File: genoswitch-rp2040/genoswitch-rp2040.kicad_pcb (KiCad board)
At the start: 2 copper layers, 37 parts, among them J1 USB_B_Micro, J2 Conn_01x03_Socket-PicoDebug, J3 HW-SPI0, J4 HW-SPI1, J5 PIO-SPI0, J6 PIO-SPI1, J7 SERIAL, SW1 PTS815_SJM_250_SMTR_LFS, U1 NCP1117-3.3_SOT223, U2 W25Q128JVS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

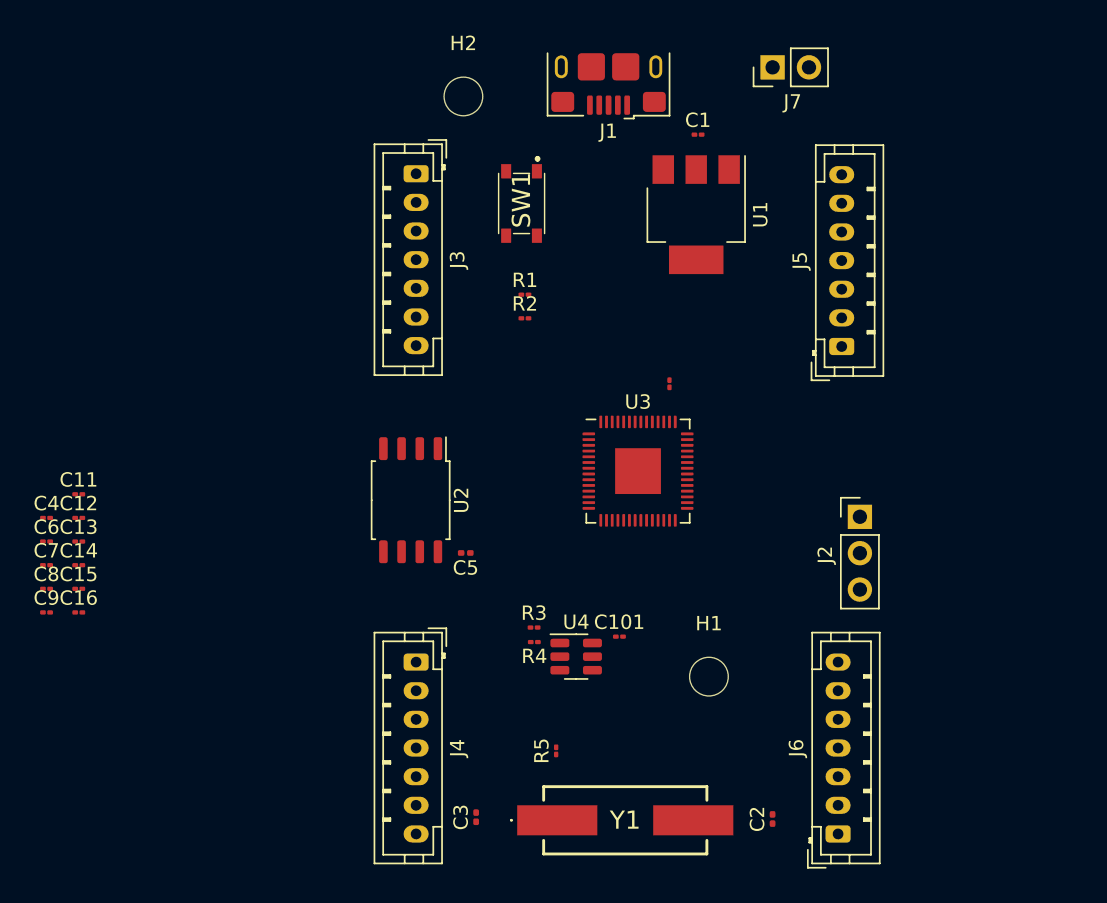
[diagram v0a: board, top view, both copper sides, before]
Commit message: Place all components in rough positions
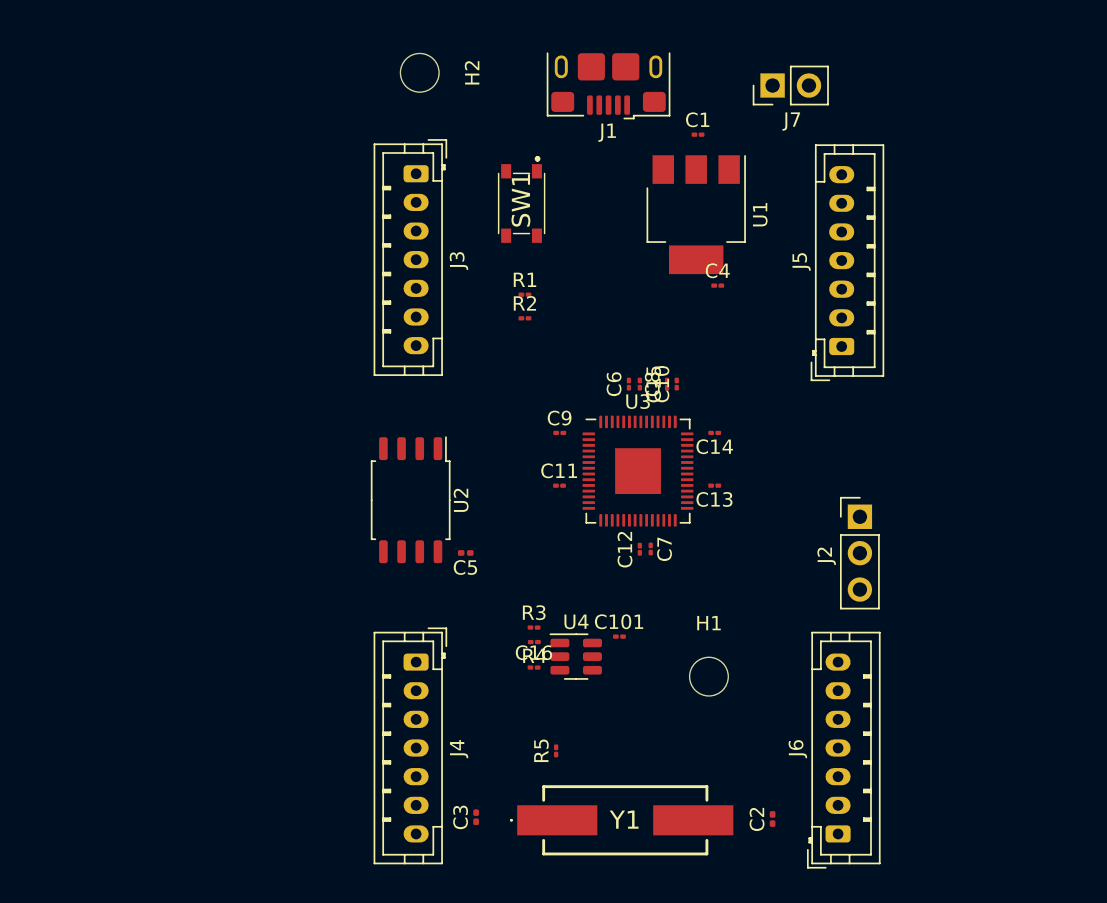
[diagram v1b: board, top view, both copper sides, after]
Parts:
- moved C4 49.6 mm to (114.9, 61.0)
- moved C8 45.6 mm to (111.4, 67.8), turned to 90 degrees
- moved C14 45.4 mm to (114.7, 71.2), turned to 180 degrees
- moved C13 44.6 mm to (114.7, 74.9), turned to 180 degrees
- moved C7 42.2 mm to (110.2, 79.4), turned to -90 degrees
- moved C6 42.1 mm to (108.7, 67.8), turned to 90 degrees
- moved C15 41.7 mm to (109.5, 67.8), turned to -90 degrees
- moved C12 39.2 mm to (109.5, 79.4), turned to 90 degrees
- moved C9 38.0 mm to (103.9, 71.2)
- moved C11 33.6 mm to (103.9, 74.9)
- moved C16 32.0 mm to (102.1, 87.6)
- moved H2 3.47 mm to (94.1, 46.1), turned to -90 degrees
- moved J7 1.27 mm to (118.7, 47.0)
- moved C10 0.51 mm to (112.1, 67.8)

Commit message: Swap to horizonal JST PH connector
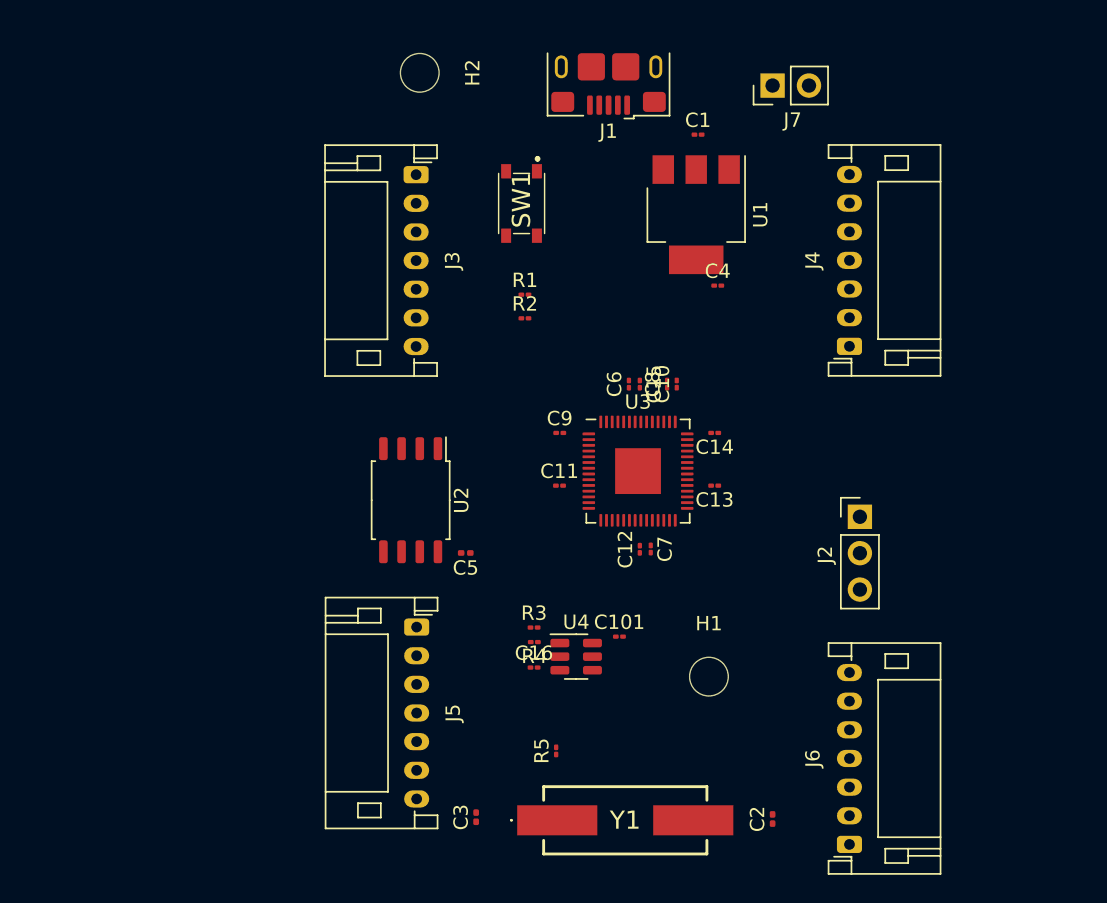
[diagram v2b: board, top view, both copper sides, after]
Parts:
- J3, J4, J5, J6: footprint Connector_JST:JST_PH_B7B-PH-K_1x07_P2.00mm_Vertical -> Connector_JST:JST_PH_S7B-PH-K_1x07_P2.00mm_Horizontal
- moved J4 37.4 mm to (124.1, 65.2), turned to 90 degrees
- moved J5 35.6 mm to (93.9, 84.8), turned to -90 degrees
- moved J6 1.08 mm to (124.1, 100.0)
- moved J3 0.06 mm to (93.9, 53.2)

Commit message: Route USB Data Lines
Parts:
- moved C15 26.3 mm to (135.8, 68.3)
- moved C6 26.3 mm to (135.1, 68.3)
- moved C8 26.3 mm to (137.7, 68.3)
- moved C10 26.3 mm to (138.4, 68.3)
- moved U1 2.13 mm to (115.2, 57.1)
- moved C1 1.44 mm to (114.3, 51.6)
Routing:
- net /USB_D+: track 0.00 -> 23.5 mm
- net /USB_D-: track 0.00 -> 23.5 mm
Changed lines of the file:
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@@
   )
   (footprint "Capacitor_SMD:C_01005_0402Metric" (layer "F.Cu")
-    (at 112.052 67.835 90)
+    (at 138.39 68.321 90)
     (descr "Capacitor SMD 01005 (0402 Metric), square (rectangular) end terminal, IPC_7351 nominal, (Body size source: http://www.vishay.com/docs/20056/crcw01005e3.pdf), generated with kicad-footprint-generator")
     (tags "capacitor")
@@
   )
   (footprint "Capacitor_SMD:C_01005_0402Metric" (layer "F.Cu")
-    (at 108.712 67.839 90)
+    (at 135.05 68.325 90)
     (descr "Capacitor SMD 01005 (0402 Metric), square (rectangular) end terminal, IPC_7351 nominal, (Body size source: http://www.vishay.com/docs/20056/crcw01005e3.pdf), generated with kicad-footprint-generator")
     (tags "capacitor")
@@
   )
   (footprint "Capacitor_SMD:C_01005_0402Metric" (layer "F.Cu")
-    (at 109.474 67.839 -90)
+    (at 135.812 68.325 -90)
     (descr "Capacitor SMD 01005 (0402 Metric), square (rectangular) end terminal, IPC_7351 nominal, (Body size source: http://www.vishay.com/docs/20056/crcw01005e3.pdf), generated with kicad-footprint-generator")
     (tags "capacitor")
@@
   )
   (footprint "Package_TO_SOT_SMD:SOT-223-3_TabPin2" (layer "F.Cu")
-    (at 113.411 56.007 -90)
+    (at 115.212 57.15 -90)
     (descr "module CMS SOT223 4 pins")
     (tags "CMS SOT")
@@
   )
   (footprint "Capacitor_SMD:C_01005_0402Metric" (layer "F.Cu")
-    (at 113.538 50.419)
+    (at 114.287 51.65)
     (descr "Capacitor SMD 01005 (0402 Metric), square (rectangular) end terminal, IPC_7351 nominal, (Body size source: http://www.vishay.com/docs/20056/crcw01005e3.pdf), generated with kicad-footprint-generator")
     (tags "capacitor")
@@
   )
   (footprint "Capacitor_SMD:C_01005_0402Metric" (layer "F.Cu")
-    (at 111.379 67.839 90)
+    (at 137.717 68.325 90)
     (descr "Capacitor SMD 01005 (0402 Metric), square (rectangular) end terminal, IPC_7351 nominal, (Body size source: http://www.vishay.com/docs/20056/crcw01005e3.pdf), generated with kicad-footprint-generator")
     (tags "capacitor")
@@
     (property "ki_keywords" "RP2040 ARM Cortex-M0+ USB")
     (attr smd)
-    (fp_text reference "U3" (at 0 -4.82) (layer "F.SilkS")
+    (fp_text reference "U3" (at 26.338 -4.334) (layer "F.SilkS")
         (effects (font (size 1 1) (thickness 0.15)))
     )
@@
     (stroke (width 0.15) (type default)) (layer "User.1"))
   (segment (start 111.544 70.4735) (end 111.547 70.4765) (width 0.15) (layer "F.Cu") (net 7))
+  (segment (start 108.162 50) (end 108.162 64.97655) (width 0.8) (layer "F.Cu") (net 10))
+  (segment (start 107.94 48.358) (end 107.94 49.778) (width 0.1524) (layer "F.Cu") (net 10))
+  (segment (start 108.162 64.97655) (end 110.965231 67.779781) (width 0.8) (layer "F.Cu") (net 10))
+  (segment (start 107.94 49.778) (end 108.162 50) (width 0.1524) (layer "F.Cu") (net 10))
+  (segment (start 110.747 70.4765) (end 110.747 69.326447) (width 0.1524) (layer "F.Cu") (net 10))
+  (segment (start 110.965231 67.779781) (end 110.965231 69.108216) (width 0.8) (layer "F.Cu") (net 10))
+  (segment (start 110.747 69.326447) (end 110.965231 69.108216) (width 0.1524) (layer "F.Cu") (net 10))
+  (segment (start 110.347 70.4765) (end 110.347 69.442385) (width 0.1524) (layer "F.Cu") (net 11))
+  (segment (start 110.347 69.442385) (end 110.012831 69.108216) (width 0.1524) (layer "F.Cu") (net 11))
+  (segment (start 107.112 65.27345) (end 110.012831 68.174281) (width 0.8) (layer "F.Cu") (net 11))
+  (segment (start 110.012831 68.174281) (end 110.012831 69.108216) (width 0.8) (layer "F.Cu") (net 11))
+  (segment (start 107.112 50) (end 107.112 65.27345) (width 0.8) (layer "F.Cu") (net 11))
+  (segment (start 107.29 48.358) (end 107.29 49.822) (width 0.1524) (layer "F.Cu") (net 11))
+  (segment (start 107.29 49.822) (end 107.112 50) (width 0.1524) (layer "F.Cu") (net 11))
 )

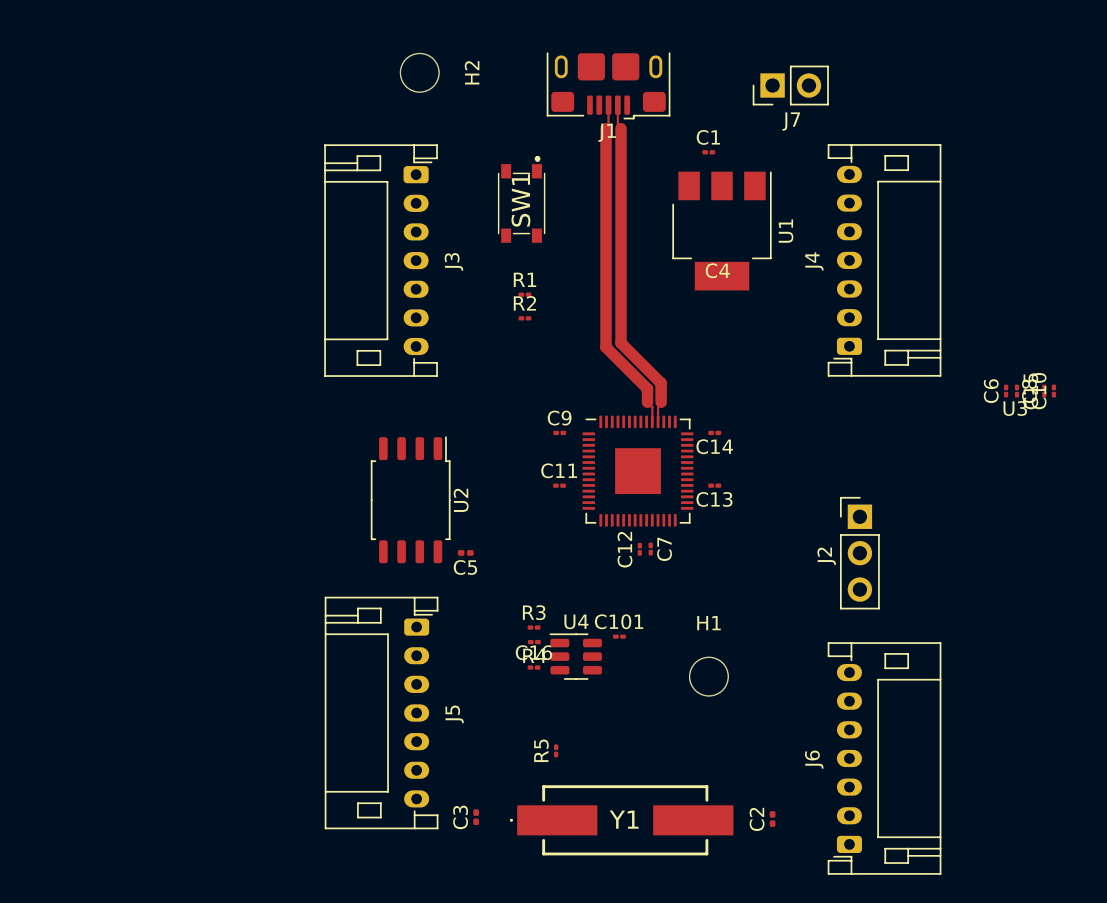
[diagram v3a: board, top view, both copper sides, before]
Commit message: move components, slight routing
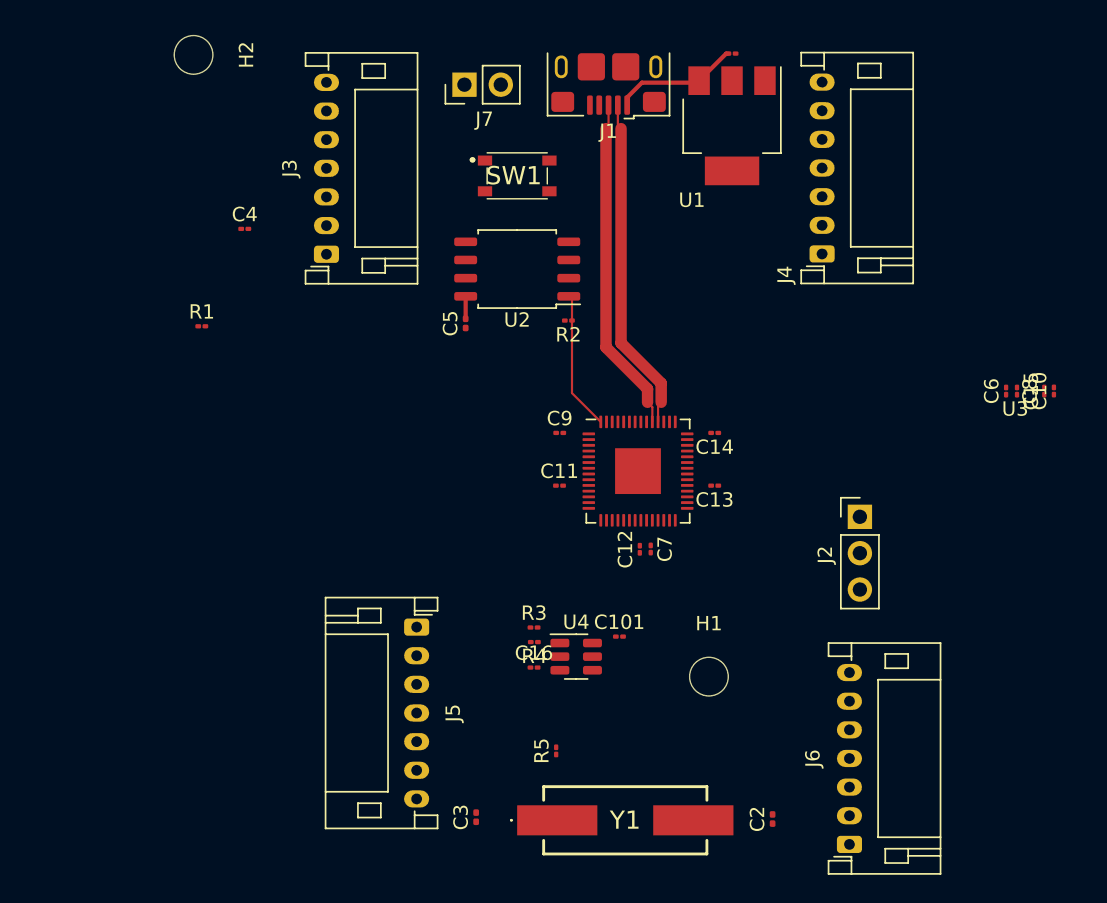
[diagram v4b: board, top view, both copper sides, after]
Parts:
- moved C4 33.3 mm to (81.9, 57.0)
- moved R1 22.7 mm to (78.9, 63.8)
- moved J7 21.5 mm to (97.2, 46.9)
- moved U2 17.8 mm to (100.9, 59.8), turned to 180 degrees
- moved C5 16.0 mm to (97.3, 63.6), turned to 90 degrees
- moved H2 15.8 mm to (78.3, 44.9)
- moved J3 8.37 mm to (87.6, 58.8), turned to 90 degrees
- moved U1 7.38 mm to (115.9, 49.8)
- moved C1 7.08 mm to (115.9, 44.8)
- moved J4 6.73 mm to (122.2, 58.8)
- moved R2 3.04 mm to (104.5, 63.4), turned to 180 degrees
- moved SW1 1.95 mm to (100.9, 53.3), turned to 0 degrees
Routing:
- net /QSPI_SS: track 0.00 -> 9.69 mm
- net VBUS: track 0.00 -> 8.88 mm
- net +3V3: track 0.00 -> 1.57 mm

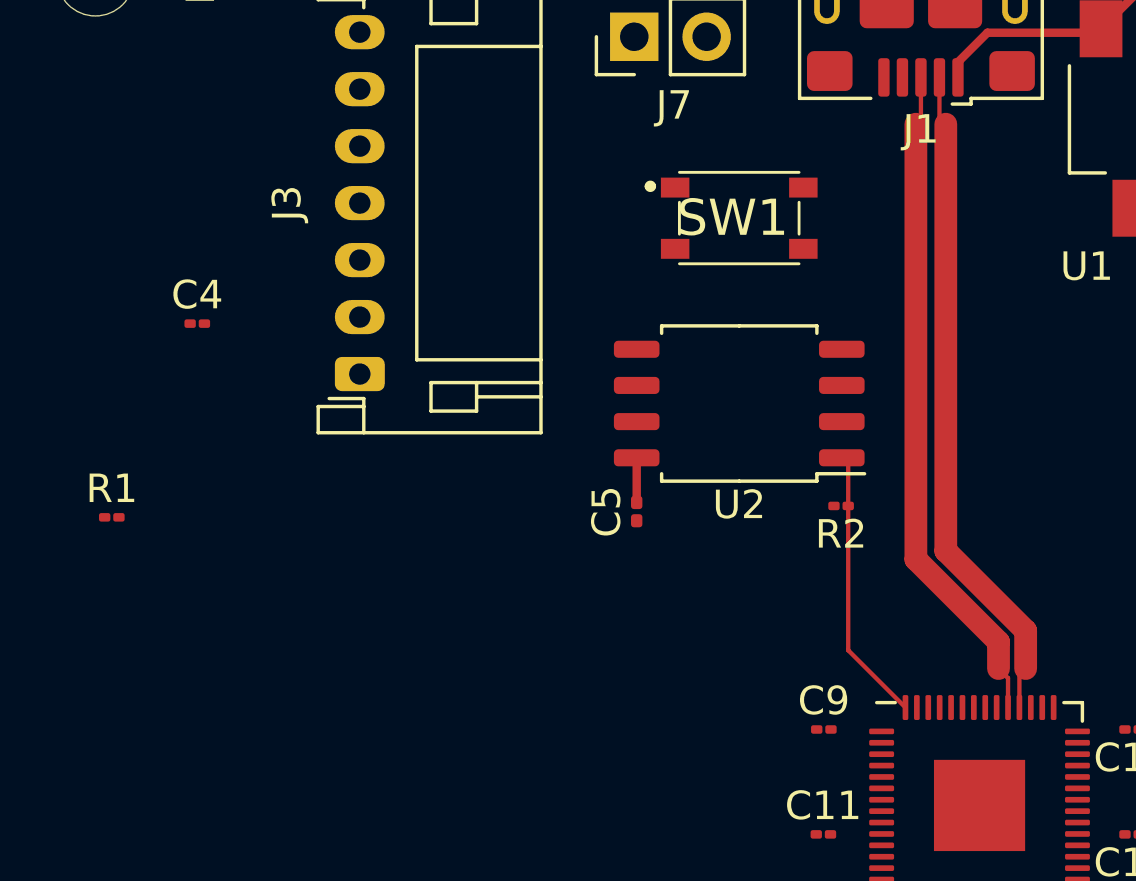
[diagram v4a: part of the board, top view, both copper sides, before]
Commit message: Route U2, SW1 -> RP2040
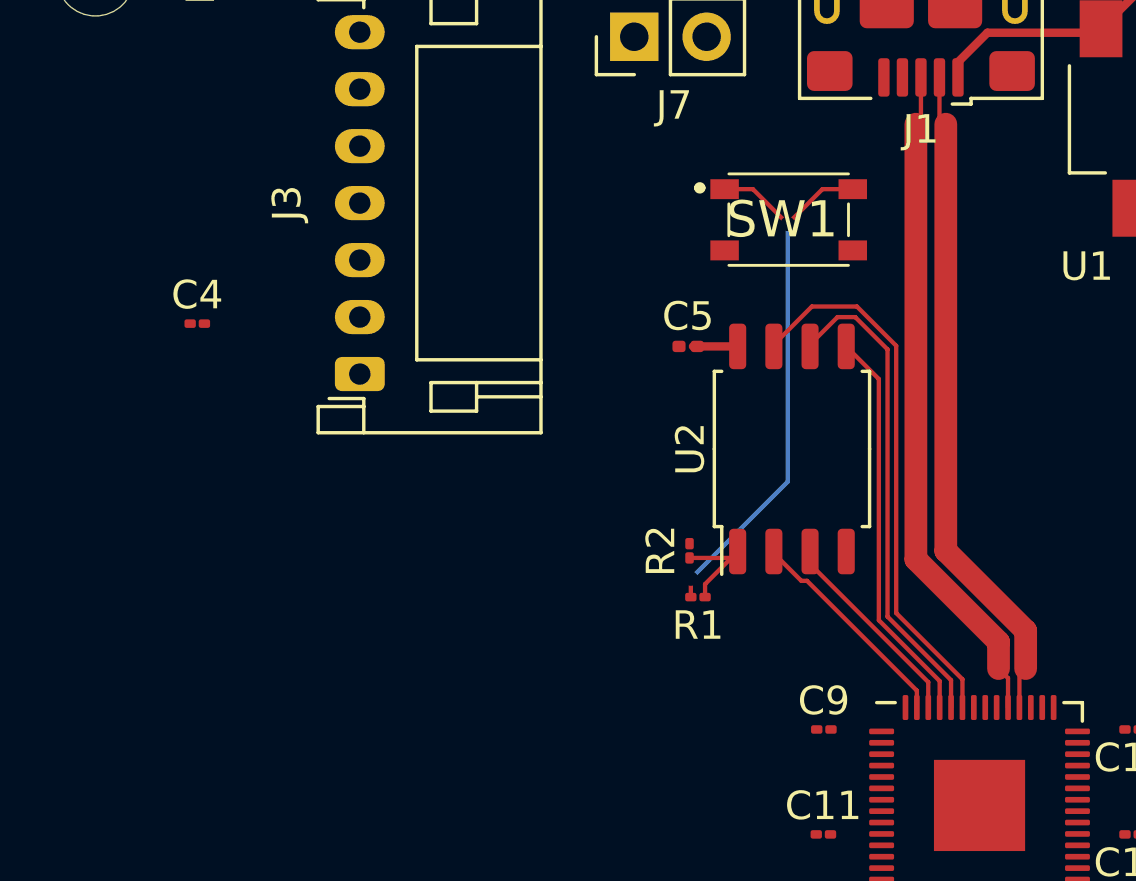
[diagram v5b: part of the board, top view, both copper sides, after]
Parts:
- moved R1 20.8 mm to (99.5, 66.6), turned to 180 degrees
- moved C5 6.07 mm to (99.1, 57.8), turned to 0 degrees
- moved R2 5.55 mm to (99.2, 65.0), turned to 90 degrees
- moved U2 2.44 mm to (102.8, 61.4), turned to 90 degrees
- moved SW1 1.74 mm to (102.6, 53.4)
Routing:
- net Net-(SW1-COM_1): track 0.00 -> 20.0 mm, vias 0 -> 2
- net /QSPI_SD3: track 0.00 -> 19.1 mm
- net /QSPI_SCLK: track 0.00 -> 17.1 mm
- net /QSPI_SD0: track 0.00 -> 14.1 mm
- net /QSPI_SD1: track 0.00 -> 7.67 mm
- net /QSPI_SD2: track 0.00 -> 7.20 mm
- net /QSPI_SS: track 9.69 -> 3.86 mm
